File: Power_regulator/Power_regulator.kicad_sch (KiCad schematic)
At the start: 19 parts, among them J1 54-00166, J1 Conn_01x02_Pin, J2 Conn_01x01_Pin, J3 Conn_01x15_Pin, Q1 NPN, Q2 NPN, Q3 NPN, Q4 NPN, Q5 NPN, U1 LM2596T-3.3/NOPB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

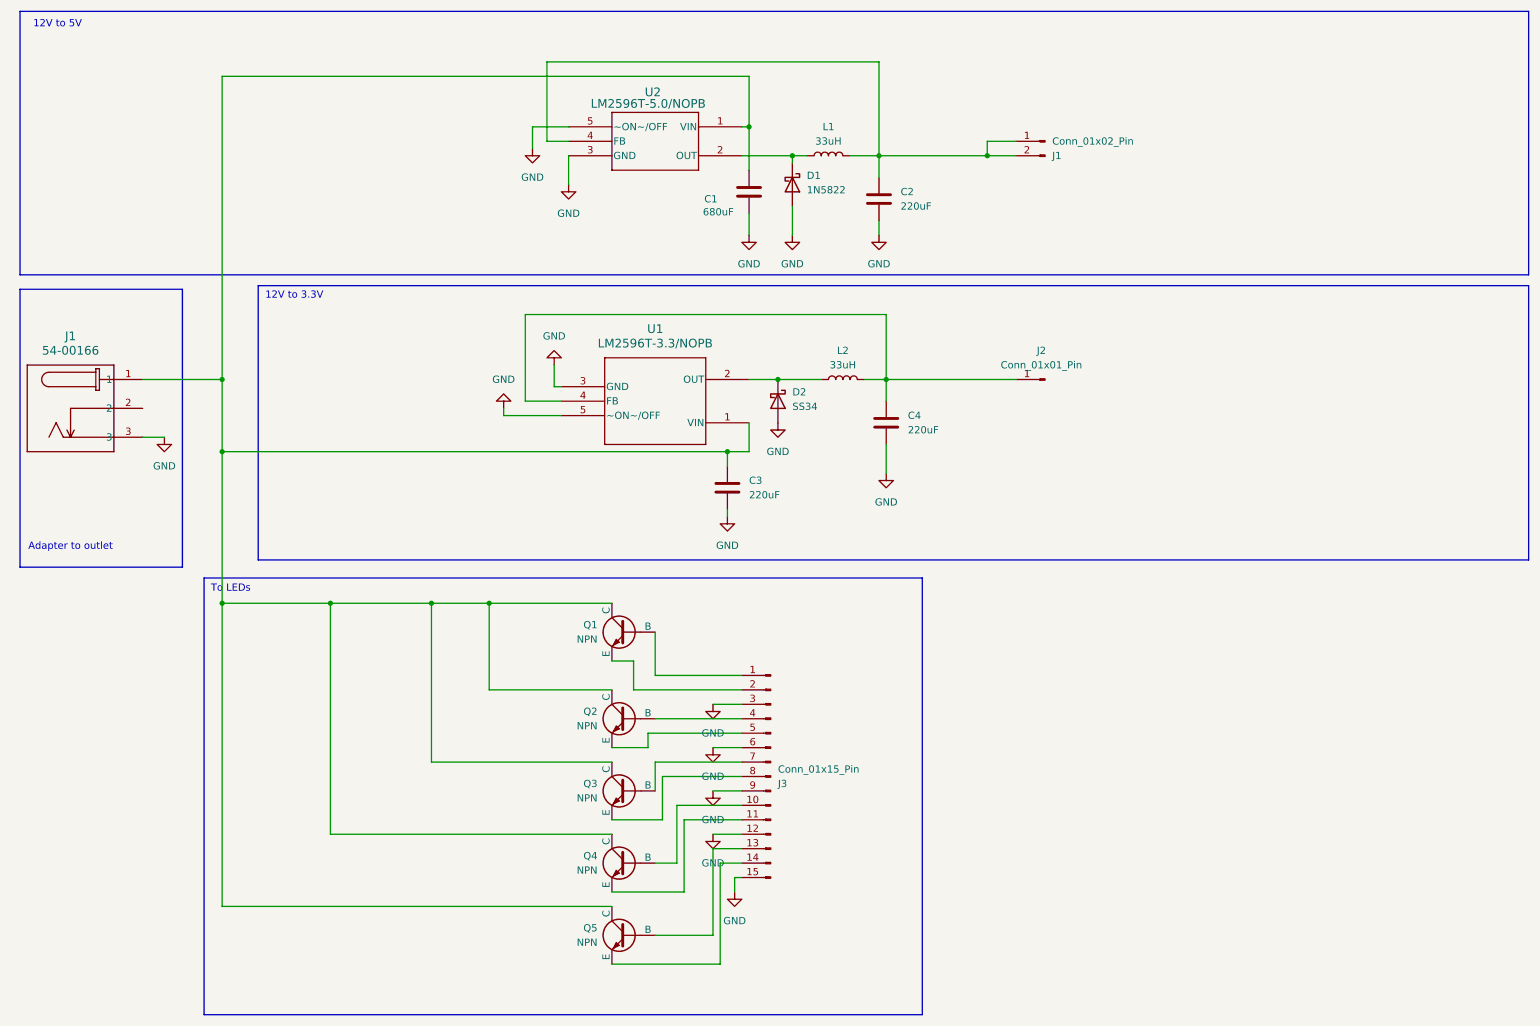
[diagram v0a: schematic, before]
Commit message: New design for power regulation circuit
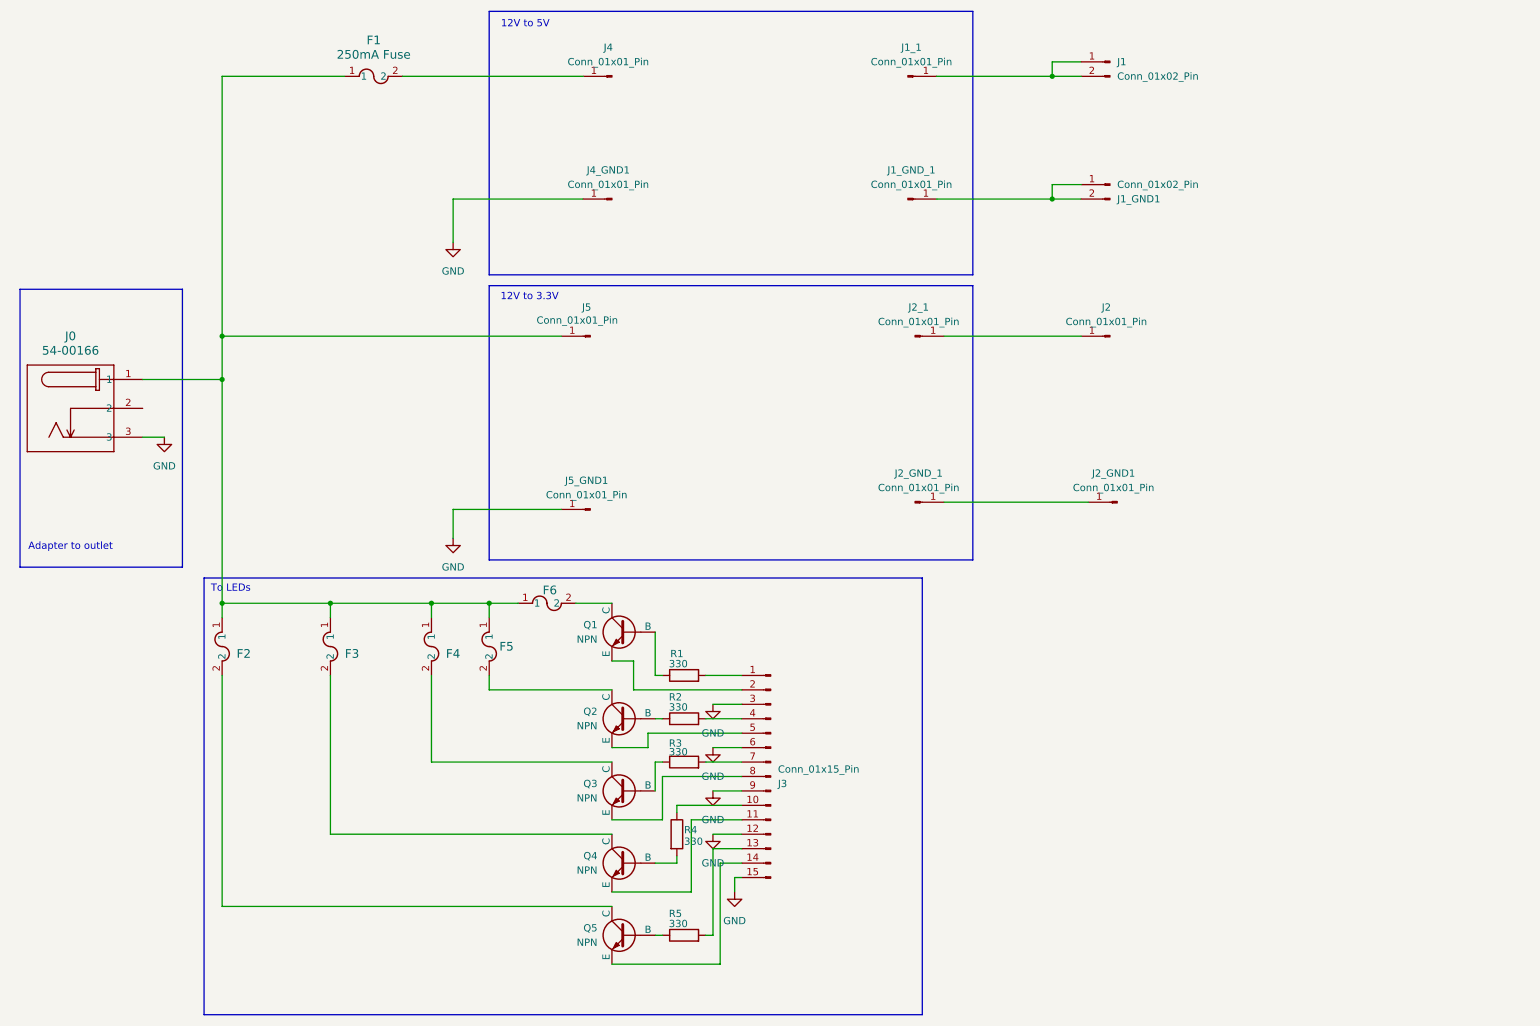
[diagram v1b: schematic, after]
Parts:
- removed C1: 680uF, symbol Device:C
- removed C2, C3, C4: 220uF, symbol Device:C
- removed D1: 1N5822, Diode_THT:D_DO-201AD_P15.24mm_Horizontal, symbol Diode:1N5822
- removed D2: SS34, Diode_SMD:D_SMA, symbol Diode:SS34
- removed L1, L2: 33uH, symbol Device:L
- removed U1: LM2596T-3.3/NOPB, T05D, symbol Power_regulator:LM2596T-3.3_NOPB
- removed U2: LM2596T-5.0/NOPB, T05D, symbol Power_regulator:LM2596T-5.0_NOPB
- added F1: 250mA Fuse, Imported Footprints:FUS_LITTELFUSE_370_LTF_250mA, symbol Power_regulator:250mA Fuse
- added F2, F3, F4, F5, F6: 100mA Fuse, Imported Footprints:FUS_LITTELFUSE_396_LTF_100mA, symbol Power_regulator:100mA Fuse
- added J1_1, J1_GND_1, J2_1, J2_GND1, J2_GND_1, J4, J4_GND1, J5, J5_GND1: Conn_01x01_Pin, Connector_PinHeader_2.54mm:PinHeader_1x01_P2.54mm_Vertical, symbol Connector:Conn_01x01_Pin
- added J1_GND1: Conn_01x02_Pin, Connector_PinHeader_2.54mm:PinHeader_1x02_P2.54mm_Vertical, symbol Connector:Conn_01x02_Pin
- added R1, R2, R3, R4, R5: 330, Resistor_THT:R_Axial_DIN0207_L6.3mm_D2.5mm_P5.08mm_Vertical, symbol Device:R
- J0: renamed from J1; footprint CONN3_54-00166_TEN -> Imported Footprints:CONN3_54-00166_TEN
- J1: footprint (none) -> Connector_PinHeader_2.54mm:PinHeader_1x02_P2.54mm_Vertical
- J2: footprint (none) -> Connector_PinHeader_2.54mm:PinHeader_1x01_P2.54mm_Vertical
- J3: footprint (none) -> Connector_PinHeader_2.54mm:PinHeader_1x15_P2.54mm_Vertical
- Q1, Q2, Q3, Q4, Q5: footprint (none) -> Imported Footprints:NPN_transistor
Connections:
- net GND: now also J4_GND1.1 (Pin_1), J5_GND1.1 (Pin_1)
- net at J1.1 (Pin_1), J1.2 (Pin_2): now also J1_1.1 (Pin_1)
- net at J2.1 (Pin_1): now also J2_1.1 (Pin_1)
- net at Q5.2 (B): now also R5.1; no longer J3.13 (Pin_13)
- net at Q3.2 (B): now also R3.1; no longer J3.7 (Pin_7)
- net at Q2.2 (B): now also R2.1; no longer J3.4 (Pin_4)
- net at Q1.2 (B): now also R1.1; no longer J3.1 (Pin_1)
- net at J3.10 (Pin_10): now also R4.1; no longer Q4.2 (B)
- new net: F1.1, F2.1, F3.1, F4.1, F5.1, F6.1, J0.1, J5.1 (Pin_1)
- new net: F1.2, J4.1 (Pin_1)
- new net: F2.2, Q5.1 (C)
- new net: J2_GND1.1 (Pin_1), J2_GND_1.1 (Pin_1)
- new net: F4.2, Q3.1 (C)
- new net: F5.2, Q2.1 (C)
- new net: Q4.2 (B), R4.2
- new net: J1_GND1.1 (Pin_1), J1_GND1.2 (Pin_2), J1_GND_1.1 (Pin_1)
- new net: J3.13 (Pin_13), R5.2
- new net: F6.2, Q1.1 (C)
- new net: J3.1 (Pin_1), R1.2
- new net: F3.2, Q4.1 (C)
- new net: J3.7 (Pin_7), R3.2
- new net: J3.4 (Pin_4), R2.2
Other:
- moved on the sheet: J2

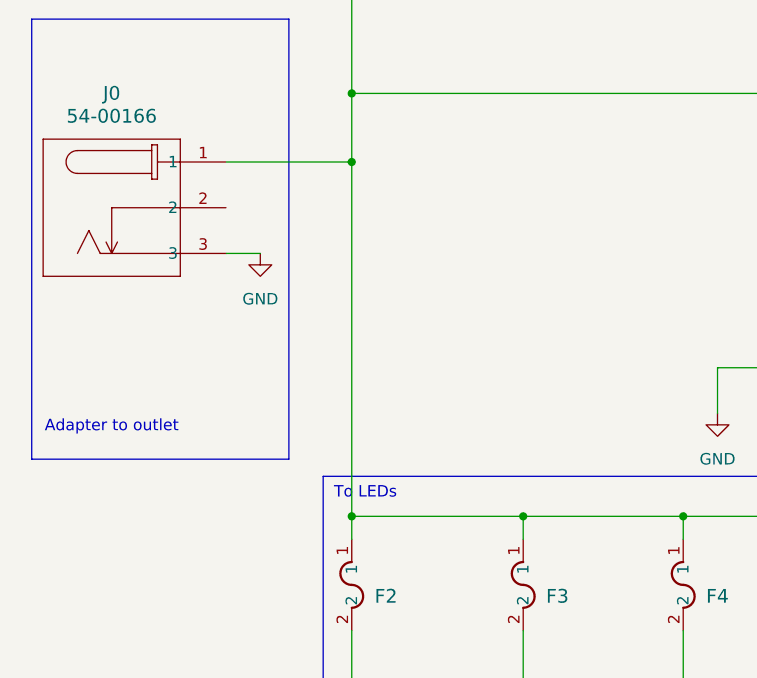
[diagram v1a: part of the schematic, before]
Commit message: Finalized design for power regulator
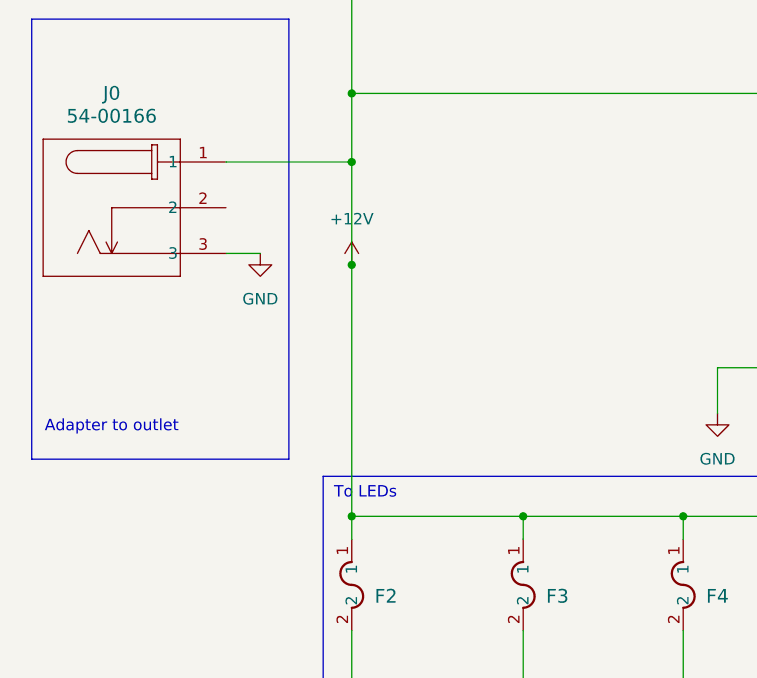
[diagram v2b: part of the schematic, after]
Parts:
- R1, R2, R3, R4, R5: footprint Resistor_THT:R_Axial_DIN0207_L6.3mm_D2.5mm_P5.08mm_Vertical -> Resistor_THT:R_Axial_DIN0204_L3.6mm_D1.6mm_P7.62mm_Horizontal
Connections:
- net +12V: now reaches F1.1, F2.1, F3.1, F4.1, F5.1, F6.1, J0.1, J5.1 (Pin_1)
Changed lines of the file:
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@@
+	)
+	(junction
+		(at 52.07 91.44)
+		(diameter 0)
+		(color 0 0 0 0)
 	)
 	(junction
@@
 	(wire
 		(pts
-			(xy 52.07 80.01) (xy 52.07 119.38)
+			(xy 52.07 80.01) (xy 52.07 91.44)
 		)
 		(stroke
@@
 		(pts
 			(xy 129.54 157.48) (xy 129.54 149.86)
+		)
+		(stroke
+			(width 0)
+			(type default)
+		)
+	)
+	(wire
+		(pts
+			(xy 52.07 91.44) (xy 52.07 119.38)
 		)
 		(stroke
@@
 	)
 	(symbol
+		(lib_id "power:+12V")
+		(at 52.07 91.44 0)
+		(unit 1)
+		(exclude_from_sim no)
+		(in_bom yes)
+		(on_board yes)
+		(dnp no)
+		(fields_autoplaced yes)
+		(property "Reference" "#PWR02"
+			(at 52.07 95.25 0)
+			(effects
+				(font
+					(size 1.27 1.27)
+				)
+				(hide yes)
+			)
+		)
+		(property "Value" "+12V"
+			(at 52.07 86.36 0)
+			(effects
+				(font
+					(size 1.27 1.27)
+				)
+			)
+		)
+		(property "Footprint" ""
+			(at 52.07 91.44 0)
+			(effects
+				(font
+					(size 1.27 1.27)
+				)
+				(hide yes)
+			)
+		)
+		(property "Datasheet" ""
+			(at 52.07 91.44 0)
+			(effects
+				(font
+					(size 1.27 1.27)
+				)
+				(hide yes)
+			)
+		)
+		(property "Description" "Power symbol creates a global label with name \"+12V\""
+			(at 52.07 91.44 0)
+			(effects
+				(font
+					(size 1.27 1.27)
+				)
+				(hide yes)
+			)
+		)
+		(pin "1"
+		)
+		(instances
+			(project ""
+				(path "/ed5e7dc3-b551-4b16-ba42-f25354774d36"
+					(reference "#PWR02")
+					(unit 1)
+				)
+			)
+		)
+	)
+	(symbol
 		(lib_id "Connector:Conn_01x01_Pin")
 		(at 120.65 26.67 180)
@@
 			)
 		)
-		(property "Footprint" "Resistor_THT:R_Axial_DIN0207_L6.3mm_D2.5mm_P5.08mm_Vertical"
+		(property "Footprint" "Resistor_THT:R_Axial_DIN0204_L3.6mm_D1.6mm_P7.62mm_Horizontal"
 			(at 130.302 160.02 90)
 			(effects
@@
 			)
 		)
-		(property "Footprint" "Resistor_THT:R_Axial_DIN0207_L6.3mm_D2.5mm_P5.08mm_Vertical"
+		(property "Footprint" "Resistor_THT:R_Axial_DIN0204_L3.6mm_D1.6mm_P7.62mm_Horizontal"
 			(at 133.35 179.578 90)
 			(effects
@@
 			)
 		)
-		(property "Footprint" "Resistor_THT:R_Axial_DIN0207_L6.3mm_D2.5mm_P5.08mm_Vertical"
+		(property "Footprint" "Resistor_THT:R_Axial_DIN0204_L3.6mm_D1.6mm_P7.62mm_Horizontal"
 			(at 133.35 133.858 90)
 			(effects
@@
 			)
 		)
-		(property "Footprint" "Resistor_THT:R_Axial_DIN0207_L6.3mm_D2.5mm_P5.08mm_Vertical"
+		(property "Footprint" "Resistor_THT:R_Axial_DIN0204_L3.6mm_D1.6mm_P7.62mm_Horizontal"
 			(at 133.35 149.098 90)
 			(effects
@@
 			)
 		)
-		(property "Footprint" "Resistor_THT:R_Axial_DIN0207_L6.3mm_D2.5mm_P5.08mm_Vertical"
+		(property "Footprint" "Resistor_THT:R_Axial_DIN0204_L3.6mm_D1.6mm_P7.62mm_Horizontal"
 			(at 133.35 141.478 90)
 			(effects

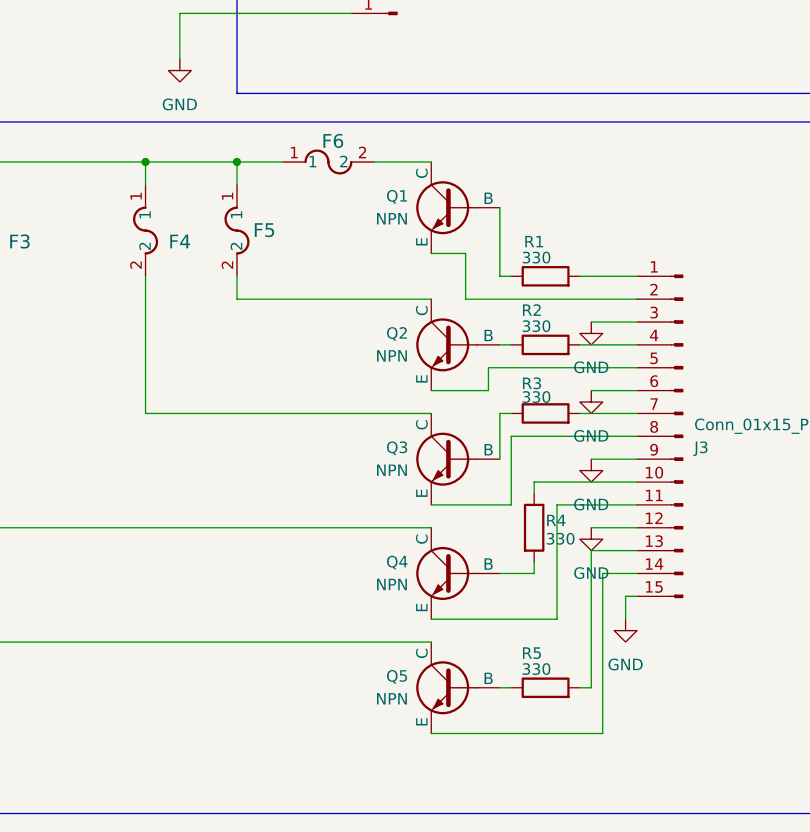
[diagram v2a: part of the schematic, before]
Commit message: Took some screenshots, changed the transistors of the power regulator
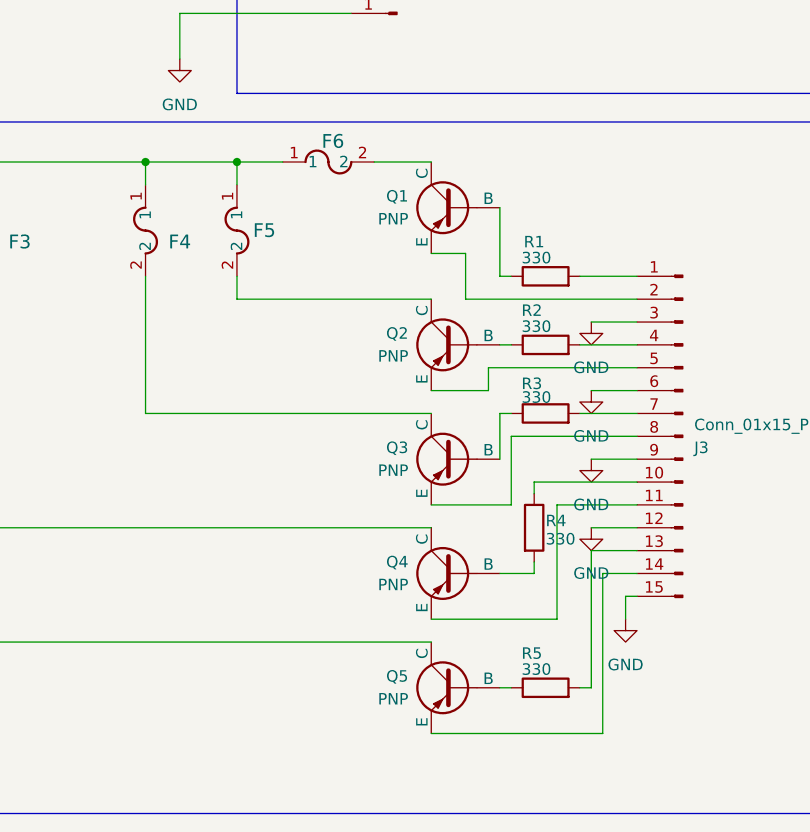
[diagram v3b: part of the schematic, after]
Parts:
- removed Q1, Q2, Q3, Q4, Q5: NPN, Imported Footprints:NPN_transistor, symbol Simulation_SPICE:NPN
- added Q1, Q2, Q3, Q4, Q5: PNP, symbol Simulation_SPICE:PNP
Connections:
- net at F2.2: now also Q5.1 (C)
- net at R5.1: now also Q5.2 (B)
- net at J3.14 (Pin_14): now also Q5.3 (E)
- net at F4.2: now also Q3.1 (C)
- net at R3.1: now also Q3.2 (B)
- net at J3.8 (Pin_8): now also Q3.3 (E)
- net at F5.2: now also Q2.1 (C)
- net at R4.2: now also Q4.2 (B)
- net at F6.2: now also Q1.1 (C)
- net at R1.1: now also Q1.2 (B)
- net at F3.2: now also Q4.1 (C)
- net at R2.1: now also Q2.2 (B)
- net at J3.5 (Pin_5): now also Q2.3 (E)
- net at J3.11 (Pin_11): now also Q4.3 (E)
- net at J3.2 (Pin_2): now also Q1.3 (E)
